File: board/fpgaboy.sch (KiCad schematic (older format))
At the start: 83 parts, among them J1 Conn_01x12, J2 Conn_01x06, J3 Micro_SD_Card_Det, J4 Conn_01x06, P1 ILI9341, P2 CONN_01X02, P3 USB_OTG, Q1 BSS816NW, SW1 SWITCH_SPST, U1 iCE40-HX8k-BG121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

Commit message: Fix ERCs on schematic (SRAM controls unconnected oops). Ready for layout!
Former-commit-id: 202b182379a01c0fb2a119a5850cd0e08c7dbe72 [formerly 86b19f6ba7559f60dbdfce0b263ec2e63d73cd75]
Former-commit-id: f6afff385088ec8977dd953ecbc976619d289004
Former-commit-id: e7fd20351cb775cefb8e5f5e2094818bde919f17
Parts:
- SW1: symbol fpgaboy-rescue:SWITCH_SPST -> fpgaboy_parts:SWITCH_SPST
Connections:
- net +5V: no longer D2.2 (A)
- net +BATT: now also D2.2 (A), SW1.1; no longer SW1.~ (2)
- net SRAM_~CE: now also U1.L2 (IOB_61)
- net SRAM_~LB: now also U1.L4 (IOB_72)
- net SRAM_~OE: now also U1.J4 (IOB_64)
- net SRAM_~UB: now also U1.L3 (IOB_71)
- net SRAM_~WE: now also U1.K3 (IOB_63)
- net at R12.1, U5.2 (EN1), U5.9 (EN2): now also SW1.2; no longer SW1.~ (2)
- net CHARGE: now reaches R11.2, U4.3 (~CHG)
- no-connect marks 57 -> 52
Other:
- note added: "Inductors:\n490-15987-1-ND\nor similar"
- note added: "Separate nets from 1V2\ndue to RC filter. Must\nexplicitly mark as powered."
- moved on the sheet: TP14
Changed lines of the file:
@@
 L fpgaboy-rescue:Tie_point TP14
 U 1 1 5A7FAA71
-P 13700 2200
-F 0 "TP14" H 13700 2300 60  0000 C CNN
-F 1 "Tie_point" H 13700 2150 60  0000 C CNN
-F 2 "fpgaboy_parts:tiepoint-0.5" H 13700 2200 60  0001 C CNN
-F 3 "" H 13700 2200 60  0001 C CNN
-	1    13700 2200
+P 13550 2250
+F 0 "TP14" H 13550 2350 60  0000 C CNN
+F 1 "Tie_point" H 13550 2200 60  0000 C CNN
+F 2 "fpgaboy_parts:tiepoint-0.5" H 13550 2250 60  0001 C CNN
+F 3 "" H 13550 2250 60  0001 C CNN
+	1    13550 2250
 	1    0    0    -1
 $EndComp
@@
 L fpgaboy-rescue:GND #PWR064
 U 1 1 5A7FD6FB
-P 13500 2350
-F 0 "#PWR064" H 13500 2100 50  0001 C CNN
-F 1 "GND" H 13500 2200 50  0000 C CNN
-F 2 "" H 13500 2350 50  0000 C CNN
-F 3 "" H 13500 2350 50  0000 C CNN
-	1    13500 2350
+P 13250 2400
+F 0 "#PWR064" H 13250 2150 50  0001 C CNN
+F 1 "GND" H 13250 2250 50  0000 C CNN
+F 2 "" H 13250 2400 50  0000 C CNN
+F 3 "" H 13250 2400 50  0000 C CNN
+	1    13250 2400
 	1    0    0    -1
 $EndComp
@@
 L fpgaboy-rescue:GNDPWR #PWR065
 U 1 1 5A7FD772
-P 13900 2350
-F 0 "#PWR065" H 13900 2150 50  0001 C CNN
-F 1 "GNDPWR" H 13900 2220 50  0000 C CNN
-F 2 "" H 13900 2300 50  0000 C CNN
-F 3 "" H 13900 2300 50  0000 C CNN
-	1    13900 2350
+P 13850 2400
+F 0 "#PWR065" H 13850 2200 50  0001 C CNN
+F 1 "GNDPWR" H 13850 2270 50  0000 C CNN
+F 2 "" H 13850 2350 50  0000 C CNN
+F 3 "" H 13850 2350 50  0000 C CNN
+	1    13850 2400
 	1    0    0    -1
 $EndComp
@@
 Connection ~ 15450 700
 Wire Wire Line
-	15300 2200 15300 2650
-Wire Wire Line
 	15050 2250 15050 2200
 Wire Wire Line
@@
 	14250 1400 14150 1400
 Wire Wire Line
-	13500 2200 13500 2350
+	13250 2250 13250 2400
 Wire Wire Line
-	13900 2200 13900 2350
+	13850 2250 13850 2400
 Wire Wire Line
 	12250 1550 12300 1550
@@
 NoConn ~ 3550 1500
 NoConn ~ 3550 1600
-NoConn ~ 3550 1700
-NoConn ~ 3550 1800
-NoConn ~ 3550 1900
-NoConn ~ 3550 2000
-NoConn ~ 3550 2100
 NoConn ~ 1550 1500
 NoConn ~ 1550 1600
@@
 	15650 1850 15800 1850
 Wire Wire Line
-	15650 2200 15650 2600
-Wire Wire Line
 	15650 700  15650 750
 Connection ~ 15650 700
@@
 NoConn ~ 1550 5350
 NoConn ~ 5800 1900
-$Comp
-L fpgaboy-rescue:PWR_FLAG #FLG03
-U 1 1 5DB439D2
-P 15800 2600
-F 0 "#FLG03" H 15800 2695 50  0001 C CNN
-F 1 "PWR_FLAG" H 15800 2780 50  0000 C CNN
-F 2 "" H 15800 2600 50  0000 C CNN
-F 3 "" H 15800 2600 50  0000 C CNN
-	1    15800 2600
-	0    1    1    0
-$EndComp
-Wire Wire Line
-	15800 2600 15650 2600
-Connection ~ 15650 2600
-Wire Wire Line
-	15650 2600 15650 2650
 Wire Wire Line
 	11350 800  11350 1550
 $Comp
-L fpgaboy-rescue:SWITCH_SPST SW1
+L fpgaboy_parts:SWITCH_SPST SW1
 U 1 1 5A7FB663
 P 11800 1550
@@
 	13000 6300 13100 6300
 Connection ~ 13000 6200
-NoConn ~ 13050 6400
+NoConn ~ 13100 6400
 Wire Wire Line
 	13100 8950 13000 8950
@@
 	1    0    0    -1
 $EndComp
-Wire Wire Line
-	10700 900  10700 1100
 $Comp
 L fpgaboy-rescue:+3V3 #PWR0103
@@
 Wire Wire Line
 	5200 2150 5200 2000
-Wire Wire Line
-	5800 2000 5200 2000
 Connection ~ 5200 2000
 Wire Wire Line
@@
 NoConn ~ 9450 10600
 NoConn ~ 9450 10700
+Text Notes 14000 2800 0    50   ~ 0
+Inductors:\n490-15987-1-ND\nor similar
+Wire Wire Line
+	10150 1000 10700 1000
+Wire Wire Line
+	10700 1000 10700 1100
+Connection ~ 10150 1000
+Text Label 10700 1750 0    50   ~ 0
+CHARGE
+Wire Wire Line
+	5200 2000 5800 2000
+Text Label 6900 3200 2    50   ~ 0
+VCCPLL0
+Text Label 6900 3000 2    50   ~ 0
+VCCPLL1
+Wire Wire Line
+	7000 3200 6900 3200
+Wire Wire Line
+	6900 3000 7000 3000
+$Comp
+L fpgaboy-rescue:PWR_FLAG #FLG0101
+U 1 1 5D104CF2
+P 7000 3000
+F 0 "#FLG0101" H 7000 3095 50  0001 C CNN
+F 1 "PWR_FLAG" V 7000 3178 50  0000 L CNN
+F 2 "" H 7000 3000 50  0000 C CNN
+F 3 "" H 7000 3000 50  0000 C CNN
+	1    7000 3000
+	0    1    1    0
+$EndComp
+$Comp
+L fpgaboy-rescue:PWR_FLAG #FLG0102
+U 1 1 5D104E0C
+P 7000 3200
+F 0 "#FLG0102" H 7000 3295 50  0001 C CNN
+F 1 "PWR_FLAG" V 7000 3378 50  0000 L CNN
+F 2 "" H 7000 3200 50  0000 C CNN
+F 3 "" H 7000 3200 50  0000 C CNN
+	1    7000 3200
+	0    1    1    0
+$EndComp
+Text Notes 6650 3550 0    50   ~ 0
+Separate nets from 1V2\ndue to RC filter. Must\nexplicitly mark as powered.
+Text Label 3300 1700 2    60   ~ 0
+SRAM_~CE
+Text Label 3300 1800 2    60   ~ 0
+SRAM_~WE
+Text Label 3300 1900 2    60   ~ 0
+SRAM_~OE
+Text Label 3300 2000 2    60   ~ 0
+SRAM_~UB
+Text Label 3300 2100 2    60   ~ 0
+SRAM_~LB
+Wire Wire Line
+	3550 1700 3300 1700
+Wire Wire Line
+	3550 1800 3300 1800
+Wire Wire Line
+	3550 1900 3300 1900
+Wire Wire Line
+	3550 2000 3300 2000
+Wire Wire Line
+	3550 2100 3300 2100
+Wire Wire Line
+	15300 2200 15300 2650
+Wire Wire Line
+	15650 2200 15650 2650
+Wire Wire Line
+	13250 2250 13350 2250
+Wire Wire Line
+	13750 2250 13850 2250
+Wire Wire Line
+	13850 2250 13850 2150
+Connection ~ 13850 2250
+Wire Wire Line
+	13250 2250 13250 2150
+Connection ~ 13250 2250
+$Comp
+L fpgaboy-rescue:PWR_FLAG #FLG0103
+U 1 1 5D5A30A0
+P 13250 2150
+F 0 "#FLG0103" H 13250 2245 50  0001 C CNN
+F 1 "PWR_FLAG" H 13250 2330 50  0000 C CNN
+F 2 "" H 13250 2150 50  0000 C CNN
+F 3 "" H 13250 2150 50  0000 C CNN
+	1    13250 2150
+	1    0    0    -1
+$EndComp
+$Comp
+L fpgaboy-rescue:PWR_FLAG #FLG0104
+U 1 1 5D5A3263
+P 13850 2150
+F 0 "#FLG0104" H 13850 2245 50  0001 C CNN
+F 1 "PWR_FLAG" H 13850 2330 50  0000 C CNN
+F 2 "" H 13850 2150 50  0000 C CNN
+F 3 "" H 13850 2150 50  0000 C CNN
+	1    13850 2150
+	1    0    0    -1
+$EndComp
 $EndSCHEMATC

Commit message: Start placing components. Fix references to kicad4 footprints. Alter BGA footprint so that vias can be placed between pads.
Former-commit-id: bd528e47238e1e5486ab4242507cff2d8ebbe877 [formerly e25b043cde048c10d5d4d75b9e60daf800c100f4]
Former-commit-id: 11b4f6d371cc355af72a2cc654ce37b7b2cdccaa
Former-commit-id: 1230468cd22565a20545bb1cbead323269b41e59
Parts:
- D1, D2: footprint Diodes_SMD:D_0805 -> LED_SMD:LED_0805_2012Metric
- J2, J4: footprint Connector_PinHeader_2.54mm:PinHeader_1x06_P2.54mm_Horizontal -> Connector_PinHeader_1.27mm:PinHeader_1x06_P1.27mm_Vertical
- L1, L2: footprint Resistors_SMD:R_0805 -> Resistor_SMD:R_0805_2012Metric
- P2: footprint Pin_Headers:Pin_Header_Straight_1x02 -> Connector_PinHeader_2.54mm:PinHeader_1x02_P2.54mm_Vertical
- Q1: footprint TO_SOT_Packages_SMD:SOT-23 -> Package_TO_SOT_SMD:SOT-23
- R1, R10, R11, R12, R16, R17, R18, R19, R2, R20, R3, R4, R5, R6, R7, R8, R9: footprint Resistors_SMD:R_0603 -> Resistor_SMD:R_0603_1608Metric
- U4: footprint TO_SOT_Packages_SMD:SOT-23-6 -> Package_TO_SOT_SMD:SOT-23-6
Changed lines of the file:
@@
 F 0 "U4" H 9500 1450 51  0000 C CNN
 F 1 "BQ21040" H 9500 850 51  0000 C CNN
-F 2 "TO_SOT_Packages_SMD:SOT-23-6" H 9500 1150 51  0001 C CNN
+F 2 "Package_TO_SOT_SMD:SOT-23-6" H 9500 1150 51  0001 C CNN
 F 3 "" H 9500 1150 51  0001 C CNN
 	1    9500 1150
@@
 F 0 "R9" V 10230 1550 50  0000 C CNN
 F 1 "10k" V 10150 1550 50  0000 C CNN
-F 2 "Resistors_SMD:R_0603" V 10080 1550 50  0001 C CNN
+F 2 "Resistor_SMD:R_0603_1608Metric" V 10080 1550 50  0001 C CNN
 F 3 "" H 10150 1550 50  0000 C CNN
 	1    10150 1550
@@
 F 0 "R10" V 10430 1550 50  0000 C CNN
 F 1 "680" V 10350 1550 50  0000 C CNN
-F 2 "Resistors_SMD:R_0603" V 10280 1550 50  0001 C CNN
+F 2 "Resistor_SMD:R_0603_1608Metric" V 10280 1550 50  0001 C CNN
 F 3 "" H 10350 1550 50  0000 C CNN
 	1    10350 1550
@@
 F 0 "D2" H 10700 1350 50  0000 C CNN
 F 1 "LED" H 10700 1150 50  0000 C CNN
-F 2 "Diodes_SMD:D_0805" H 10700 1250 50  0001 C CNN
+F 2 "LED_SMD:LED_0805_2012Metric" H 10700 1250 50  0001 C CNN
 F 3 "" H 10700 1250 50  0000 C CNN
 	1    10700 1250
@@
 F 0 "R11" V 10780 1550 50  0000 C CNN
 F 1 "680" V 10700 1550 50  0000 C CNN
-F 2 "Resistors_SMD:R_0603" V 10630 1550 50  0001 C CNN
+F 2 "Resistor_SMD:R_0603_1608Metric" V 10630 1550 50  0001 C CNN
 F 3 "" H 10700 1550 50  0000 C CNN
 	1    10700 1550
@@
 F 0 "R12" V 12380 1850 50  0000 C CNN
 F 1 "10k" V 12300 1850 50  0000 C CNN
-F 2 "Resistors_SMD:R_0603" V 12230 1850 50  0001 C CNN
+F 2 "Resistor_SMD:R_0603_1608Metric" V 12230 1850 50  0001 C CNN
 F 3 "" H 12300 1850 50  0000 C CNN
 	1    12300 1850
@@
 F 0 "L1" V 14500 700 50  0000 C CNN
 F 1 "2u2" V 14625 700 50  0000 C CNN
-F 2 "Resistors_SMD:R_0805" H 14550 700 50  0001 C CNN
+F 2 "Resistor_SMD:R_0805_2012Metric" H 14550 700 50  0001 C CNN
 F 3 "" H 14550 700 50  0000 C CNN
 	1    14550 700
@@
 F 0 "R17" V 14880 900 50  0000 C CNN
 F 1 "450k" V 14800 900 50  0000 C CNN
-F 2 "Resistors_SMD:R_0603" V 14730 900 50  0001 C CNN
+F 2 "Resistor_SMD:R_0603_1608Metric" V 14730 900 50  0001 C CNN
 F 3 "" H 14800 900 50  0000 C CNN
 	1    14800 900
@@
 F 0 "R18" V 14880 1300 50  0000 C CNN
 F 1 "100k" V 14800 1300 50  0000 C CNN
-F 2 "Resistors_SMD:R_0603" V 14730 1300 50  0001 C CNN
+F 2 "Resistor_SMD:R_0603_1608Metric" V 14730 1300 50  0001 C CNN
 F 3 "" H 14800 1300 50  0000 C CNN
 	1    14800 1300
@@
 F 0 "L2" V 14500 1850 50  0000 C CNN
 F 1 "2u2" V 14625 1850 50  0000 C CNN
-F 2 "Resistors_SMD:R_0805" H 14550 1850 50  0001 C CNN
+F 2 "Resistor_SMD:R_0805_2012Metric" H 14550 1850 50  0001 C CNN
 F 3 "" H 14550 1850 50  0000 C CNN
 	1    14550 1850
@@
 F 0 "R19" V 14880 2050 50  0000 C CNN
 F 1 "100k" V 14800 2050 50  0000 C CNN
-F 2 "Resistors_SMD:R_0603" V 14730 2050 50  0001 C CNN
+F 2 "Resistor_SMD:R_0603_1608Metric" V 14730 2050 50  0001 C CNN
 F 3 "" H 14800 2050 50  0000 C CNN
 	1    14800 2050
@@
 F 0 "R20" V 14880 2450 50  0000 C CNN
 F 1 "100k" V 14800 2450 50  0000 C CNN
-F 2 "Resistors_SMD:R_0603" V 14730 2450 50  0001 C CNN
+F 2 "Resistor_SMD:R_0603_1608Metric" V 14730 2450 50  0001 C CNN
 F 3 "" H 14800 2450 50  0000 C CNN
 	1    14800 2450
@@
 F 0 "P2" H 8450 1300 50  0000 C CNN
 F 1 "CONN_01X02" V 8550 1150 50  0000 C CNN
-F 2 "Pin_Headers:Pin_Header_Straight_1x02" H 8450 1150 50  0001 C CNN
+F 2 "Connector_PinHeader_2.54mm:PinHeader_1x02_P2.54mm_Vertical" H 8450 1150 50  0001 C CNN
 F 3 "" H 8450 1150 50  0000 C CNN
 	1    8450 1150
@@
 F 0 "R2" V 1550 9700 50  0000 C CNN
 F 1 "220" V 1500 9500 50  0000 C CNN
-F 2 "Resistors_SMD:R_0603" V 1430 9500 50  0001 C CNN
+F 2 "Resistor_SMD:R_0603_1608Metric" V 1430 9500 50  0001 C CNN
 F 3 "" H 1500 9500 50  0000 C CNN
 	1    1500 9500
@@
 F 0 "R3" V 1550 9800 50  0000 C CNN
 F 1 "220" V 1500 9600 50  0000 C CNN
-F 2 "Resistors_SMD:R_0603" V 1430 9600 50  0001 C CNN
+F 2 "Resistor_SMD:R_0603_1608Metric" V 1430 9600 50  0001 C CNN
 F 3 "" H 1500 9600 50  0000 C CNN
 	1    1500 9600
@@
 F 0 "R4" V 1550 9900 50  0000 C CNN
 F 1 "220" V 1500 9700 50  0000 C CNN
-F 2 "Resistors_SMD:R_0603" V 1430 9700 50  0001 C CNN
+F 2 "Resistor_SMD:R_0603_1608Metric" V 1430 9700 50  0001 C CNN
 F 3 "" H 1500 9700 50  0000 C CNN
 	1    1500 9700
@@
 F 0 "R5" V 1550 10000 50  0000 C CNN
 F 1 "220" V 1500 9800 50  0000 C CNN
-F 2 "Resistors_SMD:R_0603" V 1430 9800 50  0001 C CNN
+F 2 "Resistor_SMD:R_0603_1608Metric" V 1430 9800 50  0001 C CNN
 F 3 "" H 1500 9800 50  0000 C CNN
 	1    1500 9800
@@
 F 0 "Q1" H 1400 10100 50  0000 L CNN
 F 1 "BSS816NW" H 1400 10000 50  0000 L CNN
-F 2 "TO_SOT_Packages_SMD:SOT-23" H 1400 10150 50  0001 C CNN
+F 2 "Package_TO_SOT_SMD:SOT-23" H 1400 10150 50  0001 C CNN
 F 3 "" H 1200 10050 50  0000 C CNN
 	1    1200 10050
@@
 F 0 "R1" V 1030 10250 50  0000 C CNN
 F 1 "10k" V 950 10250 50  0000 C CNN
-F 2 "Resistors_SMD:R_0603" V 880 10250 50  0001 C CNN
+F 2 "Resistor_SMD:R_0603_1608Metric" V 880 10250 50  0001 C CNN
 F 3 "" H 950 10250 50  0000 C CNN
 	1    950  10250
@@
 F 0 "R16" V 14830 4200 50  0000 C CNN
 F 1 "NF" V 14750 4200 50  0000 C CNN
-F 2 "Resistors_SMD:R_0603" V 14680 4200 50  0001 C CNN
+F 2 "Resistor_SMD:R_0603_1608Metric" V 14680 4200 50  0001 C CNN
 F 3 "" H 14750 4200 50  0000 C CNN
 	1    14750 4200
@@
 F 0 "R8" V 5300 1750 50  0000 C CNN
 F 1 "10" V 5200 1750 50  0000 C CNN
-F 2 "Resistors_SMD:R_0603" V 5130 1750 50  0001 C CNN
+F 2 "Resistor_SMD:R_0603_1608Metric" V 5130 1750 50  0001 C CNN
 F 3 "" H 5200 1750 50  0000 C CNN
 	1    5200 1750
@@
 F 0 "R7" V 5100 1750 50  0000 C CNN
 F 1 "10" V 5000 1750 50  0000 C CNN
-F 2 "Resistors_SMD:R_0603" V 4930 1750 50  0001 C CNN
+F 2 "Resistor_SMD:R_0603_1608Metric" V 4930 1750 50  0001 C CNN
 F 3 "" H 5000 1750 50  0000 C CNN
 	1    5000 1750
@@
 F 0 "D1" H 3700 10550 50  0000 C CNN
 F 1 "LED" H 3700 10350 50  0000 C CNN
-F 2 "Diodes_SMD:D_0805" H 3700 10450 50  0001 C CNN
+F 2 "LED_SMD:LED_0805_2012Metric" H 3700 10450 50  0001 C CNN
 F 3 "" H 3700 10450 50  0000 C CNN
 	1    3700 10450
@@
 F 0 "R6" V 3780 10750 50  0000 C CNN
 F 1 "680" V 3700 10750 50  0000 C CNN
-F 2 "Resistors_SMD:R_0603" V 3630 10750 50  0001 C CNN
+F 2 "Resistor_SMD:R_0603_1608Metric" V 3630 10750 50  0001 C CNN
 F 3 "" H 3700 10750 50  0000 C CNN
 	1    3700 10750
@@
 F 0 "J4" H 6600 10200 50  0000 L CNN
 F 1 "Conn_01x06" V 6700 10350 50  0000 L CNN
-F 2 "Connector_PinHeader_2.54mm:PinHeader_1x06_P2.54mm_Horizontal" H 6600 10600 50  0001 C CNN
+F 2 "Connector_PinHeader_1.27mm:PinHeader_1x06_P1.27mm_Vertical" H 6600 10600 50  0001 C CNN
 F 3 "~" H 6600 10600 50  0001 C CNN
 	1    6600 10600
@@
 F 0 "J2" H 6600 9250 50  0000 L CNN
 F 1 "Conn_01x06" V 6700 9400 50  0000 L CNN
-F 2 "Connector_PinHeader_2.54mm:PinHeader_1x06_P2.54mm_Horizontal" H 6600 9650 50  0001 C CNN
+F 2 "Connector_PinHeader_1.27mm:PinHeader_1x06_P1.27mm_Vertical" H 6600 9650 50  0001 C CNN
 F 3 "~" H 6600 9650 50  0001 C CNN
 	1    6600 9650

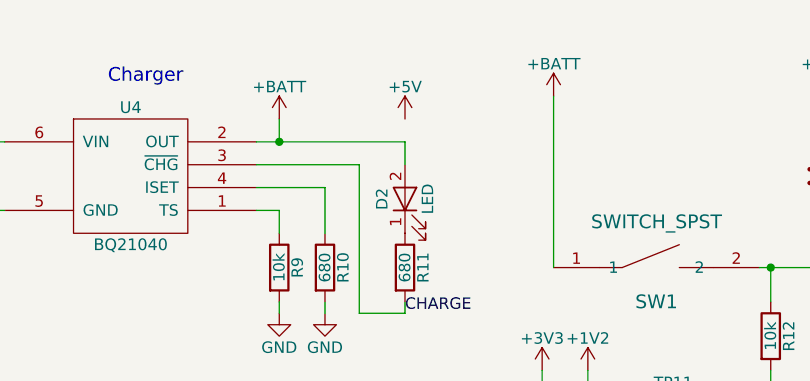
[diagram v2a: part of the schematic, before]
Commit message: First pass of placing all components.
Former-commit-id: 935330e139bbc688dd3075af15c022303e23c6e1 [formerly f9cef177abd4ecc2c663cb08782e3e3e737b028e]
Former-commit-id: 80bf02931e0e868b70c2aba9824d08be8d3d2d28
Former-commit-id: 687b3f498758089015909bee82d7bb9f30404761
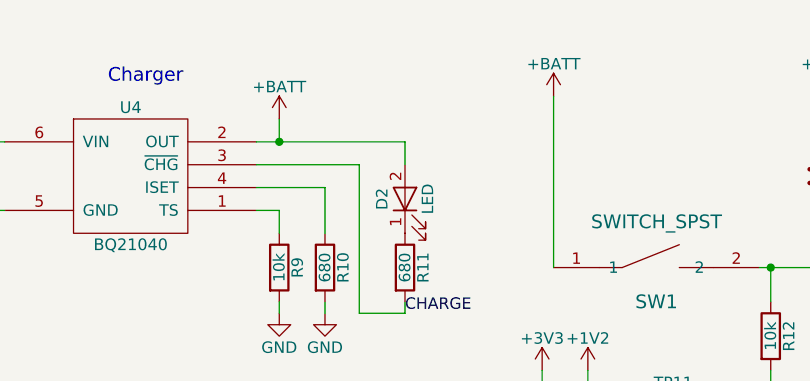
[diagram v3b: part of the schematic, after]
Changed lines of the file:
@@
 VPP_FAST for NVCM programming only.\nDo not connect.\nVPP_2V5 can be tied to 3V3 when\nnot programming NVCM.\n
-$Comp
-L fpgaboy-rescue:+5V #PWR0102
-U 1 1 5C114B8C
-P 10700 900
-F 0 "#PWR0102" H 10700 750 50  0001 C CNN
-F 1 "+5V" H 10700 1040 50  0000 C CNN
-F 2 "" H 10700 900 50  0000 C CNN
-F 3 "" H 10700 900 50  0000 C CNN
-	1    10700 900
-	1    0    0    -1
-$EndComp
 $Comp
 L fpgaboy-rescue:+3V3 #PWR0103

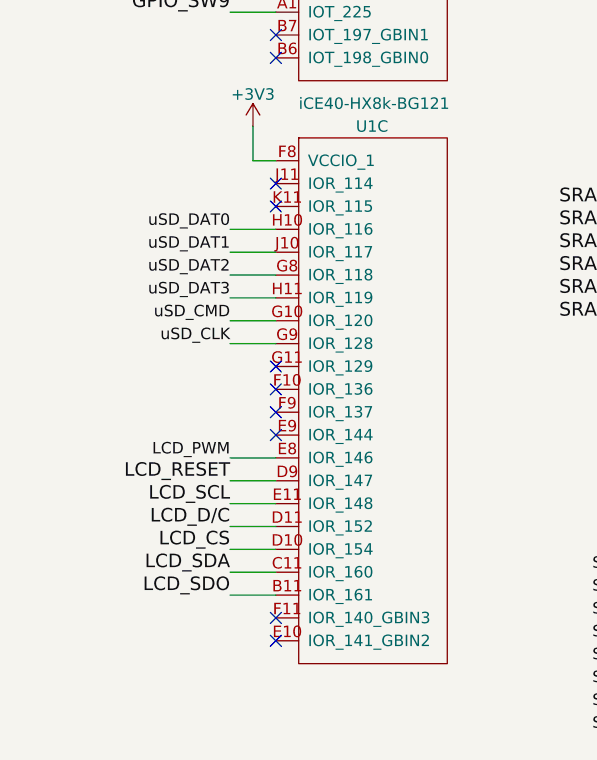
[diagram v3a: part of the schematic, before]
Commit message: Continue BGA escape. Pin-swap LCD and uSD card so that the traces don't have to cross.
Former-commit-id: f8ac038b637c7257d92a3d2f030f50e78c9c9bc2 [formerly 6bcc831231e3fdf82be743b82d14a98c5b81e0ac]
Former-commit-id: 605b2bd4fd829a74481d758a2aba6bf016992be6
Former-commit-id: 63a570fdaa14407f687558ae361da6e3eddfbbe5
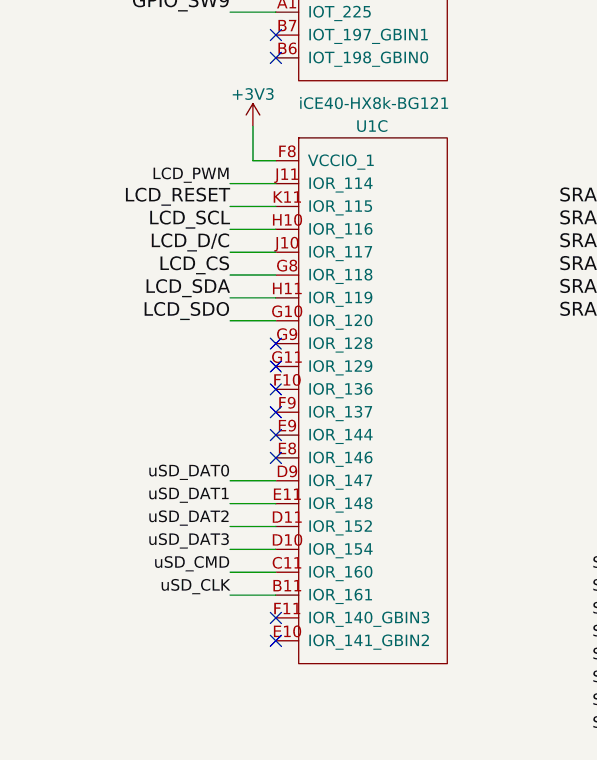
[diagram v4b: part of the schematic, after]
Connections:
- net LCD_CS: now also U1.G8 (IOR_118); no longer U1.D10 (IOR_154)
- net LCD_D/C: now also U1.J10 (IOR_117); no longer U1.D11 (IOR_152)
- net LCD_PWM: now also U1.J11 (IOR_114); no longer U1.E8 (IOR_146)
- net LCD_RESET: now also U1.K11 (IOR_115); no longer U1.D9 (IOR_147)
- net LCD_SCL: now also U1.H10 (IOR_116); no longer U1.E11 (IOR_148)
- net LCD_SDA: now also U1.H11 (IOR_119); no longer U1.C11 (IOR_160)
- net LCD_SDO: now also U1.G10 (IOR_120); no longer U1.B11 (IOR_161)
- net uSD_CLK: now also U1.B11 (IOR_161); no longer U1.G9 (IOR_128)
- net uSD_CMD: now also U1.C11 (IOR_160); no longer U1.G10 (IOR_120)
- net uSD_DAT0: now also U1.D9 (IOR_147); no longer U1.H10 (IOR_116)
- net uSD_DAT1: now also U1.E11 (IOR_148); no longer U1.J10 (IOR_117)
- net uSD_DAT2: now also U1.D11 (IOR_152); no longer U1.G8 (IOR_118)
- net uSD_DAT3: now also U1.D10 (IOR_154); no longer U1.H11 (IOR_119)
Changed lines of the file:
@@
 Text Label 3300 6650 2    50   ~ 0
 SRAM_A17
-Text Label 1350 5550 2    59   ~ 0
+Text Label 1350 4350 2    59   ~ 0
 LCD_RESET
-Text Label 1350 5650 2    59   ~ 0
+Text Label 1350 4450 2    59   ~ 0
 LCD_SCL
-Text Label 1350 5750 2    59   ~ 0
+Text Label 1350 4550 2    59   ~ 0
 LCD_D/C
-Text Label 1350 5850 2    59   ~ 0
+Text Label 1350 4650 2    59   ~ 0
 LCD_CS
-Text Label 1350 5950 2    59   ~ 0
+Text Label 1350 4750 2    59   ~ 0
 LCD_SDA
-Text Label 1350 6050 2    59   ~ 0
+Text Label 1350 4850 2    59   ~ 0
 LCD_SDO
 Wire Wire Line
-	1550 6050 1350 6050
-Wire Wire Line
-	1550 5550 1350 5550
-Wire Wire Line
-	1550 5650 1350 5650
-Wire Wire Line
-	1550 5750 1350 5750
-Wire Wire Line
-	1550 5850 1350 5850
-Wire Wire Line
-	1550 5950 1350 5950
-Wire Wire Line
-	1550 5450 1350 5450
-Text Label 1350 5450 2    50   ~ 0
+	1550 4850 1350 4850
+Wire Wire Line
+	1550 4350 1350 4350
+Wire Wire Line
+	1550 4450 1350 4450
+Wire Wire Line
+	1550 4550 1350 4550
+Wire Wire Line
+	1550 4650 1350 4650
+Wire Wire Line
+	1550 4750 1350 4750
+Wire Wire Line
+	1550 4250 1350 4250
+Text Label 1350 4250 2    50   ~ 0
 LCD_PWM
 Wire Wire Line
@@
 	1    0    0    -1
 $EndComp
-NoConn ~ 1550 4250
-NoConn ~ 1550 4350
 $Comp
 L fpgaboy-rescue:+3V3 #PWR011
@@
 FPGA decoupling
 Wire Wire Line
-	1550 4450 1350 4450
-Wire Wire Line
-	1550 4550 1350 4550
-Wire Wire Line
-	1550 4650 1350 4650
-Wire Wire Line
-	1550 4750 1350 4750
-Wire Wire Line
-	1550 4850 1350 4850
-Wire Wire Line
-	1550 4950 1350 4950
-Text Label 1350 4450 2    50   ~ 0
+	1550 5550 1350 5550
+Wire Wire Line
+	1550 5650 1350 5650
+Wire Wire Line
+	1550 5750 1350 5750
+Wire Wire Line
+	1550 5850 1350 5850
+Wire Wire Line
+	1550 5950 1350 5950
+Wire Wire Line
+	1550 6050 1350 6050
+Text Label 1350 5550 2    50   ~ 0
 uSD_DAT0
-Text Label 1350 4550 2    50   ~ 0
+Text Label 1350 5650 2    50   ~ 0
 uSD_DAT1
-Text Label 1350 4650 2    50   ~ 0
+Text Label 1350 5750 2    50   ~ 0
 uSD_DAT2
-Text Label 1350 4750 2    50   ~ 0
+Text Label 1350 5850 2    50   ~ 0
 uSD_DAT3
-Text Label 1350 4850 2    50   ~ 0
+Text Label 1350 5950 2    50   ~ 0
 uSD_CMD
-Text Label 1350 4950 2    50   ~ 0
+Text Label 1350 6050 2    50   ~ 0
 uSD_CLK
-NoConn ~ 1550 5050
+NoConn ~ 1550 5450
 NoConn ~ 1550 5150
 NoConn ~ 1550 5250
@@
 	1    0    0    -1
 $EndComp
+NoConn ~ 1550 4950
+NoConn ~ 1550 5050
 $EndSCHEMATC
